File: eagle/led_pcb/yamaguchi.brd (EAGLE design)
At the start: 20 x 20 mm, 8 parts

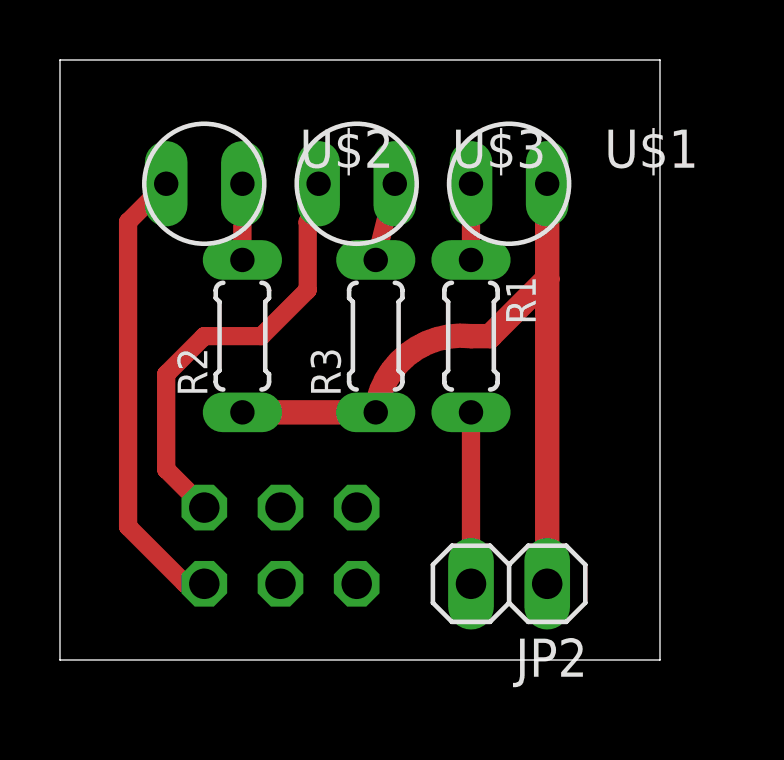
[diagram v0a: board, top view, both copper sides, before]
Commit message: led基板の配線の修正
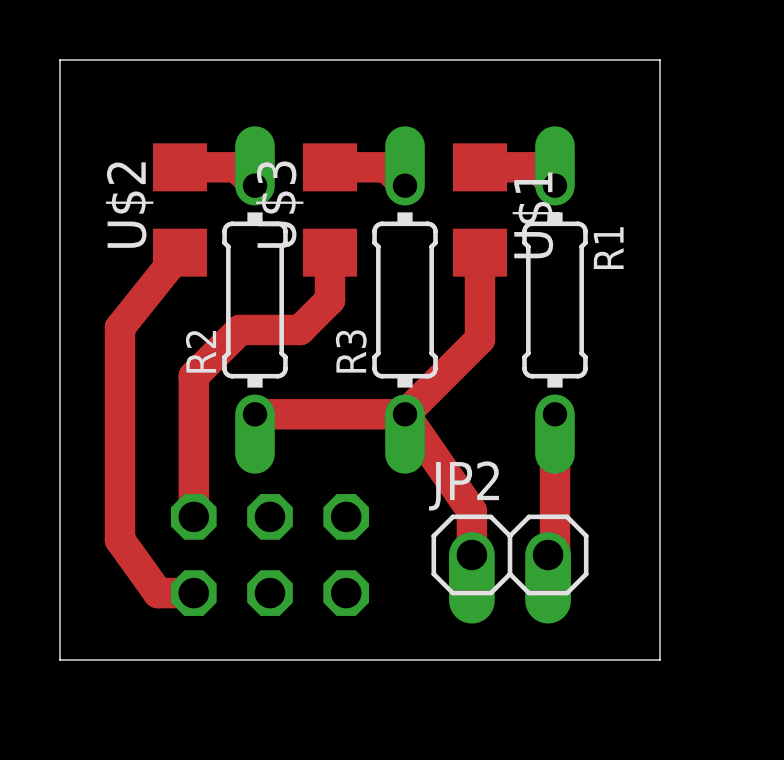
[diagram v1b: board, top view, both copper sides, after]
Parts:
- JP2: value (none) -> PINHD-1X2; device pinhead:1X02 -> Yamaguchi:1X02
- R1, R2, R3: value RES_5MM -> RES_7MM; device Yamaguchi:0204/5 -> Yamaguchi:0204/7
- U$1, U$2, U$3: value LED -> (none); device Yamaguchi:5MM -> 01_EasyAccessLib:1206
- moved R1 3.05 mm to (16.5, 12.0)
- moved R3 1.55 mm to (11.5, 12.0)
- moved U$1 1.31 mm to (14.0, 15.0), turned to 270 degrees
- moved R2 1.28 mm to (6.50, 12.0)
- moved U$3 1.25 mm to (9.00, 15.0), turned to 90 degrees
- moved U$2 1.19 mm to (4.00, 15.0), turned to 90 degrees
- moved JP2 0.96 mm to (15.0, 3.50), turned to 0 degrees
- moved JP1 0.47 mm to (7.00, 3.50)
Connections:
- net GND: now also U$1.2; no longer U$1.OUT
- net N$2: now also U$1.1; no longer U$1.IN
- net N$4: now also U$2.2; no longer U$2.OUT
- net N$5: now also U$3.2; no longer U$3.OUT
- net N$6: now also U$3.1; no longer U$3.IN
- net N$7: now also U$2.1; no longer U$2.IN
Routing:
- net GND: track 25.2 -> 16.8 mm
- net N$6: track 14.5 -> 12.4 mm
- net N$7: track 15.3 -> 13.6 mm
- net N$1: track 5.72 -> 4.79 mm
